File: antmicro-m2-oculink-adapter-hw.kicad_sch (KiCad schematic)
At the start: 10 parts, among them J2 PCB-Edge_M.2_Key-M, J3 OCuLink_x4_Amphenol_G14A42121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

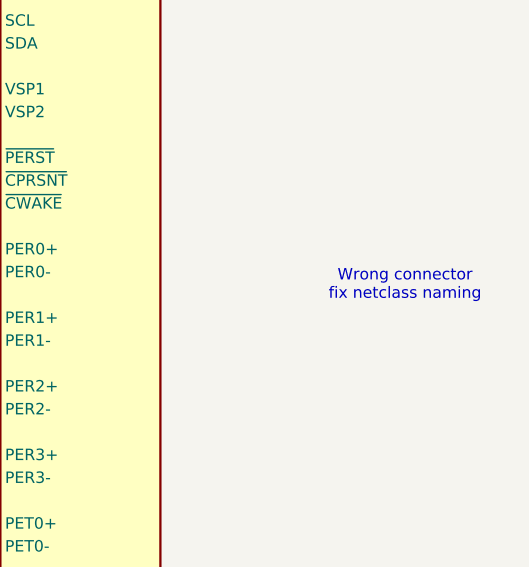
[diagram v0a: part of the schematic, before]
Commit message: [#79281] Remove unnecessary text on schematic
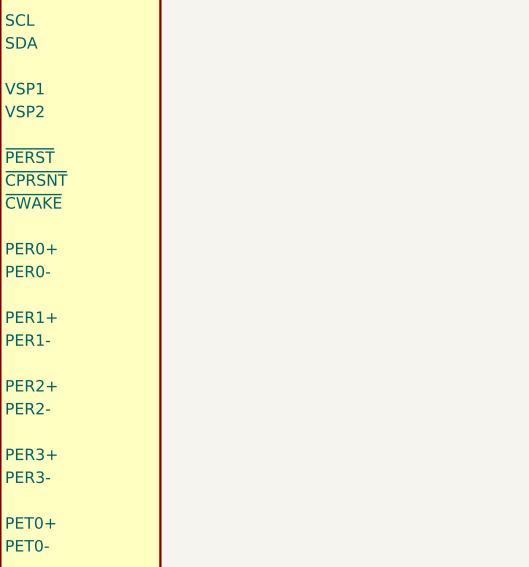
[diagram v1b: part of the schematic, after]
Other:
- note removed: "Wrong connector fix netclass naming"
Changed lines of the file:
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@@
 		(comment 1 "www.antmicro.com")
-	)
-	(text "Wrong connector \nfix netclass naming\n\n"
-		(exclude_from_sim no)
-		(at 298.958 92.71 0)
-		(effects
-			(font
-				(size 1.27 1.27)
-			)
-		)
 	)
 	(junction

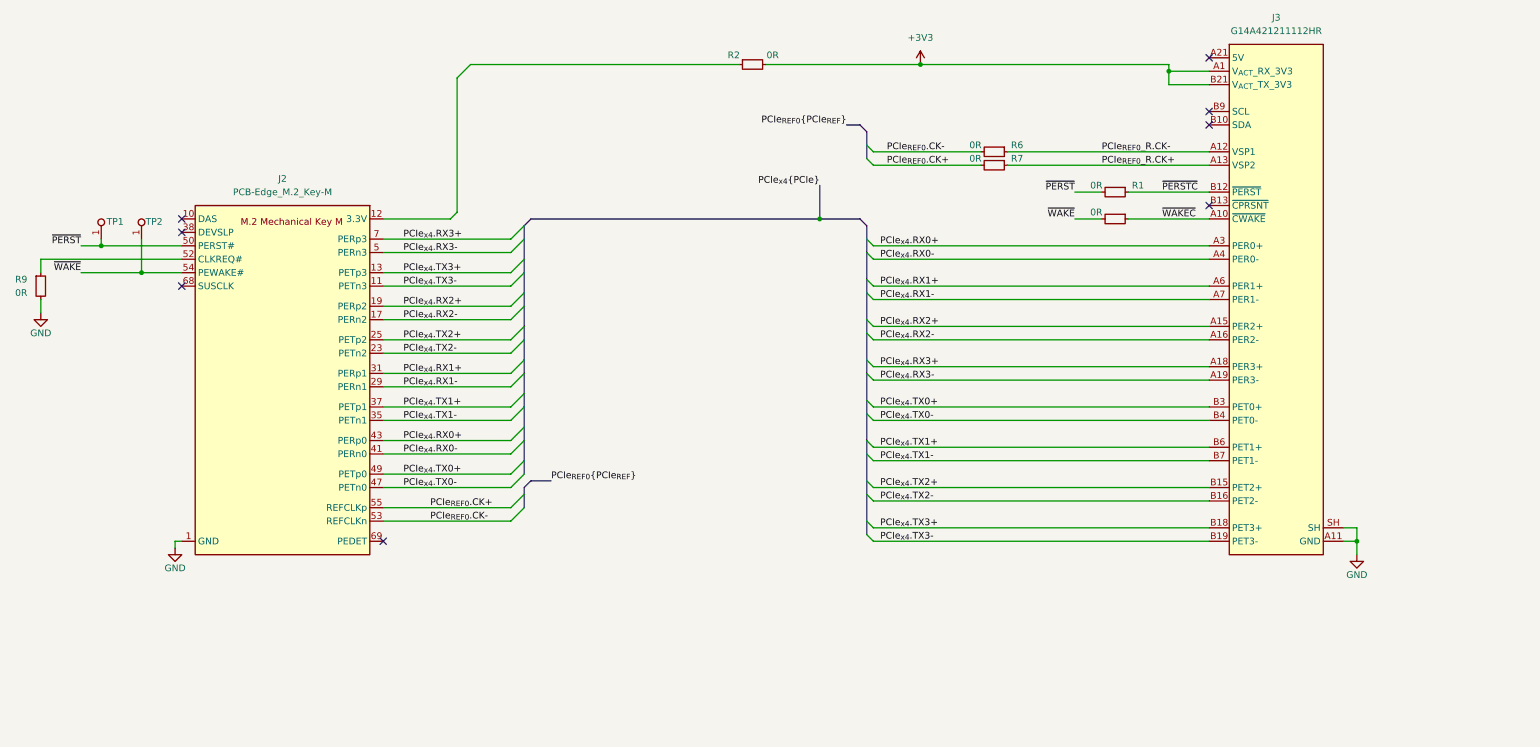
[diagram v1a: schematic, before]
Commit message: [#79281] Change 0R sizing, add OSHW logo, route 3.3V rail and control signals
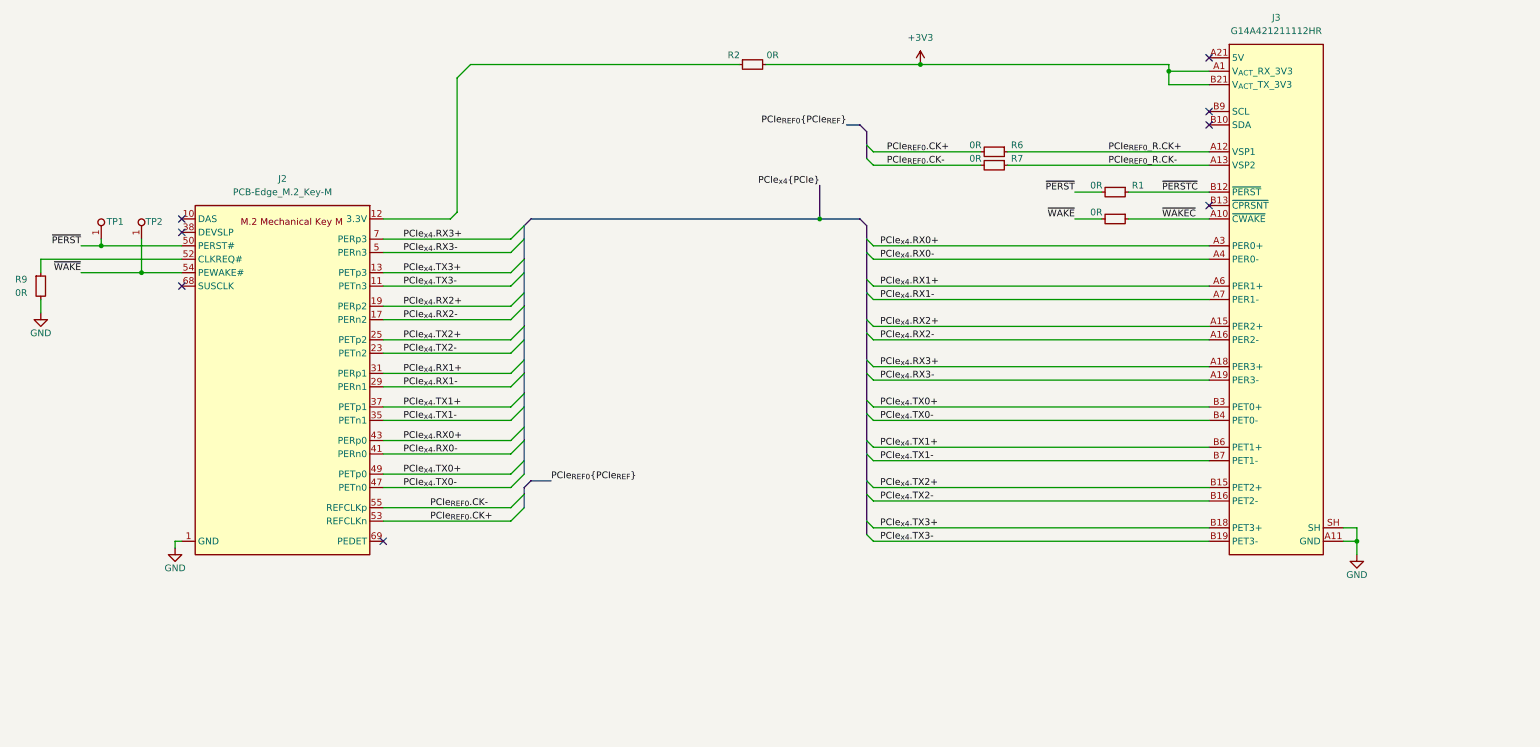
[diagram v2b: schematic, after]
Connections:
- net PCIe_{REF0}.CK+: now also J2.53 (REFCLKn), R6.2; no longer J2.55 (REFCLKp), R7.2
- net PCIe_{REF0}.CK-: now also J2.55 (REFCLKp), R7.2; no longer J2.53 (REFCLKn), R6.2
- net PCIe_{REF0}_R.CK+: now also J3.A12 (VSP1), R6.1; no longer J3.A13 (VSP2), R7.1
- net PCIe_{REF0}_R.CK-: now also J3.A13 (VSP2), R7.1; no longer J3.A12 (VSP1), R6.1
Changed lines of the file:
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@@
-		)
-	)
-	(label "PCIe_{REF0}.CK-"
-		(at 189.23 69.85 0)
-		(effects
-			(font
-				(size 1.27 1.27)
-			)
-			(justify left bottom)
 		)
 	)
@@
 		)
 	)
-	(label "PCIe_{REF0}.CK+"
-		(at 189.23 72.39 0)
-		(effects
-			(font
-				(size 1.27 1.27)
-			)
-			(justify left bottom)
-		)
-	)
 	(label "PCIe_{x4}.RX1-"
 		(at 97.79 114.3 0)
@@
 	)
 	(label "PCIe_{REF0}.CK-"
-		(at 102.87 139.7 0)
+		(at 102.87 137.16 0)
+		(effects
+			(font
+				(size 1.27 1.27)
+			)
+			(justify left bottom)
+		)
+	)
+	(label "PCIe_{REF0}_R.CK-"
+		(at 231.14 72.39 0)
 		(effects
 			(font
@@
 		)
 	)
+	(label "PCIe_{REF0}.CK-"
+		(at 189.23 72.39 0)
+		(effects
+			(font
+				(size 1.27 1.27)
+			)
+			(justify left bottom)
+		)
+	)
 	(label "PCIe_{x4}.RX3-"
 		(at 97.79 88.9 0)
@@
 	)
 	(label "PCIe_{REF0}.CK+"
-		(at 102.87 137.16 0)
+		(at 102.87 139.7 0)
 		(effects
 			(font
@@
 		)
 	)
+	(label "PCIe_{REF0}.CK+"
+		(at 189.23 69.85 0)
+		(effects
+			(font
+				(size 1.27 1.27)
+			)
+			(justify left bottom)
+		)
+	)
 	(label "~{PERST}"
 		(at 224.79 77.47 180)
@@
 		)
 	)
-	(label "PCIe_{REF0}_R.CK+"
-		(at 229.87 72.39 0)
-		(effects
-			(font
-				(size 1.27 1.27)
-			)
-			(justify left bottom)
-		)
-	)
 	(label "PCIe_{x4}.RX0+"
 		(at 97.79 124.46 0)
@@
 		)
 	)
+	(label "PCIe_{REF0}_R.CK+"
+		(at 231.14 69.85 0)
+		(effects
+			(font
+				(size 1.27 1.27)
+			)
+			(justify left bottom)
+		)
+	)
 	(label "PCIe_{x4}.TX1-"
 		(at 97.79 120.65 0)
@@
 		(effects
 			(font
-				(size 1.27 1.27)
-			)
-			(justify left bottom)
-		)
-	)
-	(label "PCIe_{REF0}_R.CK-"
-		(at 229.87 69.85 0)
-		(effects
-			(font

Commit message: [#79281] Fix schematic annotation
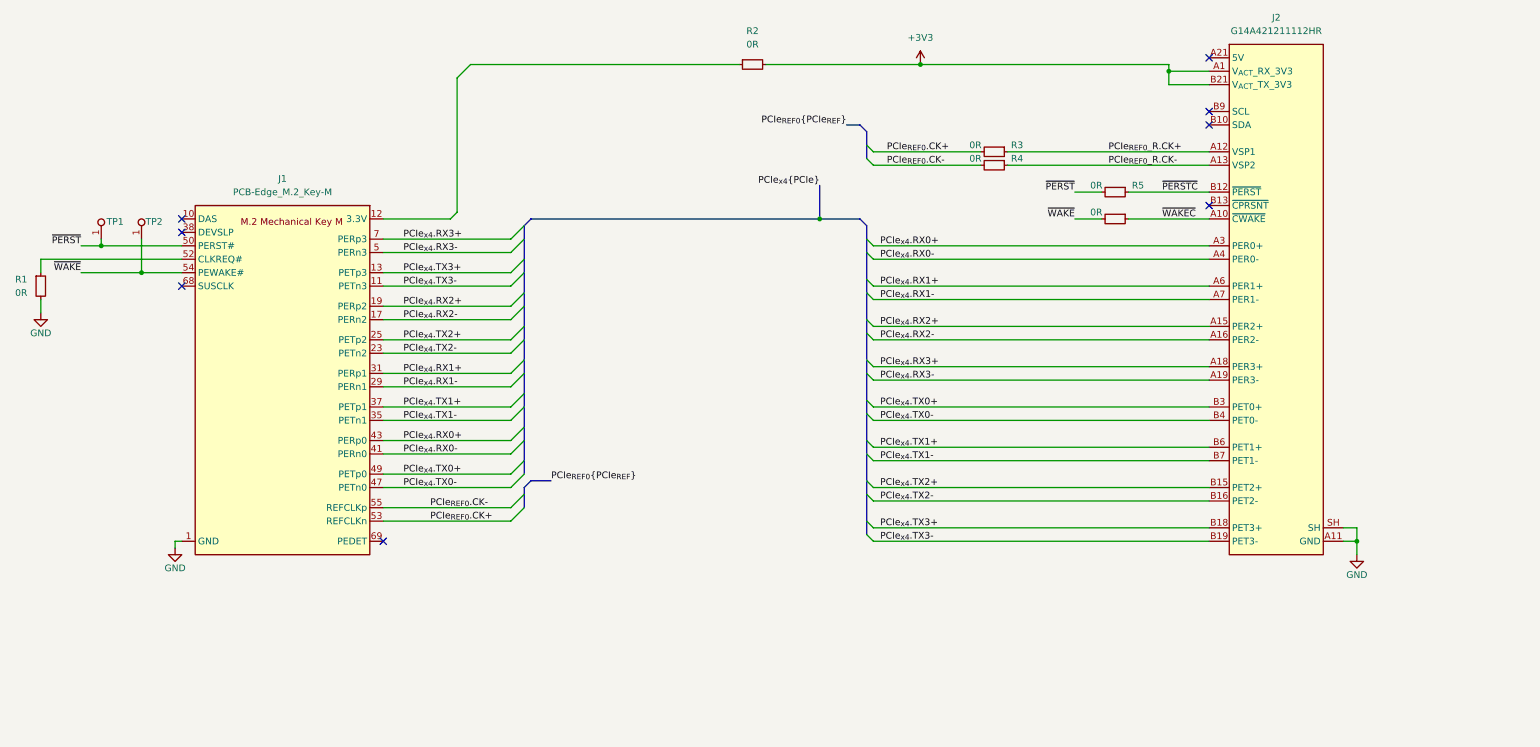
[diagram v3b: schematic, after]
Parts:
- removed R2: R_0R_0805, antmicro-footprints:R_0805_2012Metric, symbol Resistorsmisc:R_0R_0805
- added R2: R_0R_0402, antmicro-footprints:R_0402_1005Metric, symbol Resistors0402:R_0R_0402
- renumbered J2 to J1, J3 to J2, R9 to R1, R6 to R3, R7 to R4, R1 to R5, R3 to R6
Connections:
- net +3V3: now also R2.2
- net at J1.12 (3.3V), J1.14 (3.3V), J1.16 (3.3V)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: now also R2.1
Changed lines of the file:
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@@
 		(on_board yes)
 		(dnp no)
-		(property "Reference" "R6"
+		(property "Reference" "R3"
 			(at 213.868 68.58 0)
 			(effects
@@
 			(project "antmicro-m2-oculink-adapter-hw"
 				(path "/b9cca87b-aef2-493b-be4f-d9e02584eafa"
-					(reference "R6")
+					(reference "R3")
 					(unit 1)
 				)
@@
 		(on_board yes)
 		(dnp no)
-		(property "Reference" "#PWR01"
+		(property "Reference" "#PWR04"
 			(at 287.02 148.59 0)
 			(effects
@@
 			(project "antmicro-m2-oculink-adapter-hw"
 				(path "/b9cca87b-aef2-493b-be4f-d9e02584eafa"
-					(reference "#PWR01")
+					(reference "#PWR04")
 					(unit 1)
 				)
@@
 		(on_board yes)
 		(dnp no)
-		(property "Reference" "R1"
+		(property "Reference" "R5"
 			(at 236.728 76.2 0)
 			(effects
@@
 			(project "antmicro-m2-oculink-adapter-hw"
 				(path "/b9cca87b-aef2-493b-be4f-d9e02584eafa"
-					(reference "R1")
+					(reference "R5")
 					(unit 1)
 				)
@@
 		(dnp no)
 		(fields_autoplaced yes)
-		(property "Reference" "J2"
+		(property "Reference" "J1"
 			(at 74.93 74.93 0)
 			(effects
@@
 			(project ""
 				(path "/b9cca87b-aef2-493b-be4f-d9e02584eafa"
-					(reference "J2")
+					(reference "J1")
+					(unit 1)
+				)
+			)
+		)
+	)
+	(symbol
+		(lib_id "Resistors0402:R_0R_0402")
+		(at 161.29 53.34 0)
+		(unit 1)
+		(exclude_from_sim no)
+		(in_bom yes)
+		(on_board yes)
+		(dnp no)
+		(fields_autoplaced yes)
+		(property "Reference" "R2"
+			(at 163.83 46.99 0)
+			(effects
+				(font
+					(size 1.27 1.27)
+					(thickness 0.15)
+				)
+			)
+		)
+		(property "Value" "R_0R_0402"
+			(at 181.61 66.04 0)
+			(effects
+				(font
+					(size 1.27 1.27)
+					(thickness 0.15)
+				)
+				(justify left bottom)
+				(hide yes)
+			)
+		)
+		(property "Footprint" "antmicro-footprints:R_0402_1005Metric"
+			(at 181.61 68.58 0)
+			(effects
+				(font
+					(size 1.27 1.27)
+					(thickness 0.15)
+				)
+				(justify left bottom)
+				(hide yes)
+			)
+		)
+		(property "Datasheet" "https://industrial.panasonic.com/cdbs/www-data/pdf/RDA0000/AOA0000C301.pdf"
+			(at 181.61 71.12 0)
+			(effects
+				(font
+					(size 1.27 1.27)
+					(thickness 0.15)
+				)
+				(justify left bottom)
+				(hide yes)
+			)
+		)
+		(property "Description" "SMD Chip Resistor, Jumper, 0 ohm, 100 mW, 0402 [1005 Metric], Thick Film, General Purpose"
+			(at 161.29 53.34 0)
+			(effects
+				(font
+					(size 1.27 1.27)
+				)
+				(hide yes)
+			)
+		)
+		(property "MPN" "ERJ2GE0R00X"
+			(at 181.61 73.66 0)
+			(effects
+				(font
+					(size 1.27 1.27)
+					(thickness 0.15)
+				)
+				(justify left bottom)
+				(hide yes)
+			)
+		)
+		(property "Manufacturer" "Panasonic"
+			(at 181.61 76.2 0)
+			(effects
+				(font
+					(size 1.27 1.27)
+					(thickness 0.15)
+				)
+				(justify left bottom)
+				(hide yes)
+			)
+		)
+		(property "License" "Apache-2.0"
+			(at 181.61 78.74 0)
+			(effects
+				(font
+					(size 1.27 1.27)
+					(thickness 0.15)
+				)
+				(justify left bottom)
+				(hide yes)
+			)
+		)
+		(property "Author" "Antmicro"
+			(at 181.61 81.28 0)
+			(effects
+				(font
+					(size 1.27 1.27)
+					(thickness 0.15)
+				)
+				(justify left bottom)
+				(hide yes)
+			)
+		)
+		(property "Val" "0R"
+			(at 163.83 49.53 0)
+			(effects
+				(font
+					(size 1.27 1.27)
+					(thickness 0.15)
+				)
+			)
+		)
+		(property "Tolerance" "~"
+			(at 181.61 63.5 0)
+			(effects
+				(font
+					(size 1.27 1.27)
+				)
+				(justify left bottom)
+				(hide yes)
+			)
+		)
+		(property "Current" "1A"
+			(at 181.61 83.82 0)
+			(effects
+				(font
+					(size 1.27 1.27)
+					(thickness 0.15)
+				)
+				(justify left bottom)
+				(hide yes)
+			)
+		)
+		(pin "2"
+		)
+		(pin "1"
+		)
+		(instances
+			(project ""
+				(path "/b9cca87b-aef2-493b-be4f-d9e02584eafa"
+					(reference "R2")
 					(unit 1)
 				)
@@
 		(dnp no)
 		(fields_autoplaced yes)
-		(property "Reference" "R9"
+		(property "Reference" "R1"
 			(at 26.67 93.98 90)
 			(effects
@@
 			(project "antmicro-m2-oculink-adapter-hw"
 				(path "/b9cca87b-aef2-493b-be4f-d9e02584eafa"
-					(reference "R9")
+					(reference "R1")
 					(unit 1)
 				)
@@
 		(dnp no)
 		(fields_autoplaced yes)
-		(property "Reference" "#PWR04"
+		(property "Reference" "#PWR03"
 			(at 210.82 53.34 0)
 			(effects
@@
 			(project ""
 				(path "/b9cca87b-aef2-493b-be4f-d9e02584eafa"
-					(reference "#PWR04")
+					(reference "#PWR03")
 					(unit 1)
 				)
@@
 		(on_board yes)
 		(dnp no)
-		(property "Reference" "R3"
+		(property "Reference" "R6"
 			(at 236.728 81.28 0)
 			(effects
@@
 			(project "antmicro-m2-oculink-adapter-hw"
 				(path "/b9cca87b-aef2-493b-be4f-d9e02584eafa"
-					(reference "R3")
+					(reference "R6")
 					(unit 1)
 				)
@@
 		(on_board yes)
 		(dnp no)
-		(property "Reference" "R7"
+		(property "Reference" "R4"
 			(at 213.868 71.12 0)
 			(effects
@@
 			(project "antmicro-m2-oculink-adapter-hw"
 				(path "/b9cca87b-aef2-493b-be4f-d9e02584eafa"
-					(reference "R7")
+					(reference "R4")
 					(unit 1)
 				)
@@
 	)
 	(symbol
-		(lib_id "Resistorsmisc:R_0R_0805")
-		(at 161.29 53.34 0)
-		(unit 1)
-		(exclude_from_sim no)
-		(in_bom yes)
-		(on_board yes)
-		(dnp no)
-		(property "Reference" "R2"
-			(at 160.274 51.562 0)
-			(effects
-				(font
-					(size 1.27 1.27)
-					(thickness 0.15)
-				)
-			)
-		)
-		(property "Value" "R_0R_0805"
-			(at 181.61 66.04 0)
-			(effects
-				(font
-					(size 1.27 1.27)
-					(thickness 0.15)
-				)
-				(justify left bottom)
-				(hide yes)
-			)
-		)
-		(property "Footprint" "antmicro-footprints:R_0805_2012Metric"
-			(at 181.61 68.58 0)
-			(effects
-				(font
-					(size 1.27 1.27)
-					(thickness 0.15)
-				)
-				(justify left bottom)
-				(hide yes)
-			)
-		)
-		(property "Datasheet" "https://www.vishay.com/docs/20035/dcrcwe3.pdf"
-			(at 181.61 71.12 0)
-			(effects
-				(font
-					(size 1.27 1.27)
-					(thickness 0.15)
-				)
-				(justify left bottom)
-				(hide yes)
-			)
-		)
-		(property "Description" "Zero Ohm Resistor, Jumper, 0805 [2012 Metric], Thick Film, 125 mW, 2.5 A, Surface Mount Device"
-			(at 161.29 53.34 0)
-			(effects
-				(font
-					(size 1.27 1.27)
-				)
-				(hide yes)
-			)
-		)
-		(property "MPN" "CRCW08050000Z0EA"
-			(at 181.61 73.66 0)
-			(effects
-				(font
-					(size 1.27 1.27)
-					(thickness 0.15)
-				)
-				(justify left bottom)
-				(hide yes)
-			)
-		)
-		(property "Manufacturer" "Vishay"
-			(at 181.61 76.2 0)
-			(effects
-				(font
-					(size 1.27 1.27)
-					(thickness 0.15)
-				)
-				(justify left bottom)
-				(hide yes)
-			)
-		)
-		(property "License" "Apache-2.0"
-			(at 181.61 78.74 0)
-			(effects
-				(font
-					(size 1.27 1.27)
-					(thickness 0.15)
-				)
-				(justify left bottom)
-				(hide yes)
-			)
-		)
-		(property "Author" "Antmicro"
-			(at 181.61 81.28 0)
-			(effects
-				(font
-					(size 1.27 1.27)
-					(thickness 0.15)
-				)
-				(justify left bottom)
-				(hide yes)
-			)
-		)
-		(property "Val" "0R"
-			(at 167.64 51.562 0)
-			(effects
-				(font
-					(size 1.27 1.27)
-					(thickness 0.15)
-				)
-			)
-		)
-		(property "Tolerance" "~"
-			(at 181.61 63.5 0)
-			(effects
-				(font
-					(size 1.27 1.27)
-				)
-				(justify left bottom)
-				(hide yes)
-			)
-		)
-		(property "Current" "2.5A"
-			(at 181.61 83.82 0)
-			(effects
-				(font
-					(size 1.27 1.27)
-					(thickness 0.15)
-				)
-				(justify left bottom)
-				(hide yes)
-			)
-		)
-		(pin "1"
-		)
-		(pin "2"
-		)
-		(instances
-			(project ""
-				(path "/b9cca87b-aef2-493b-be4f-d9e02584eafa"
-					(reference "R2")
-					(unit 1)
-				)
-			)
-		)
-	)
-	(symbol
 		(lib_id "antmicropower:GND")
 		(at 29.21 100.33 0)
@@
 		(on_board yes)
 		(dnp no)
-		(property "Reference" "#PWR03"
+		(property "Reference" "#PWR01"
 			(at 20.32 102.87 0)
 			(effects
@@
 			(project "antmicro-m2-oculink-adapter-hw"
 				(path "/b9cca87b-aef2-493b-be4f-d9e02584eafa"
-					(reference "#PWR03")
+					(reference "#PWR01")
 					(unit 1)
 				)
@@
 		(dnp no)
 		(fields_autoplaced yes)
-		(property "Reference" "J3"
+		(property "Reference" "J2"
 			(at 262.89 44.45 0)
 			(effects
@@
 			(project ""
 				(path "/b9cca87b-aef2-493b-be4f-d9e02584eafa"
-					(reference "J3")
+					(reference "J2")
 					(unit 1)
 				)
